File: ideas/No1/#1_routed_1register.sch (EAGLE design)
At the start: 20 parts, among them P1-O8RIGHT TD620831A, P1-P8LEFT TD620831A, U1 SN74HC595N, U2 SN74HC595N, U3 SN74HC595N

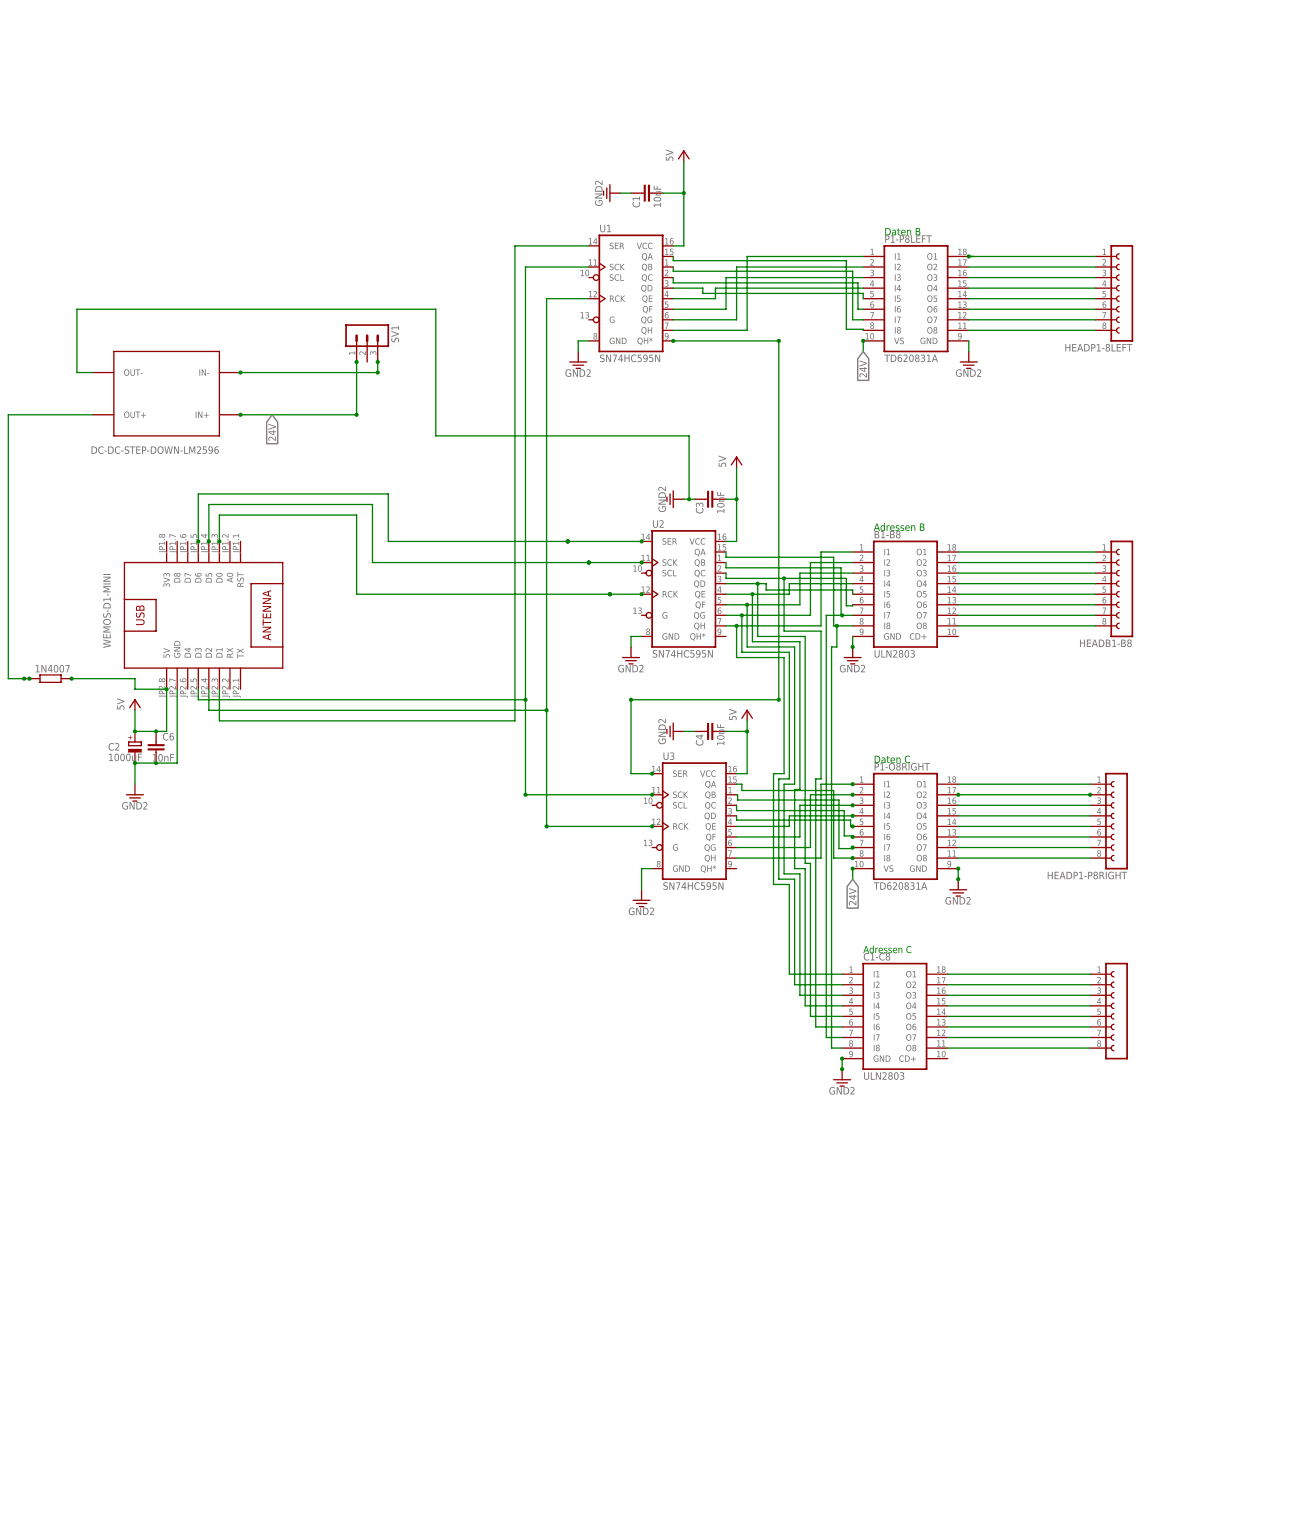
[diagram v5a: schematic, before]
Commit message: 1_route_1register.sch changed
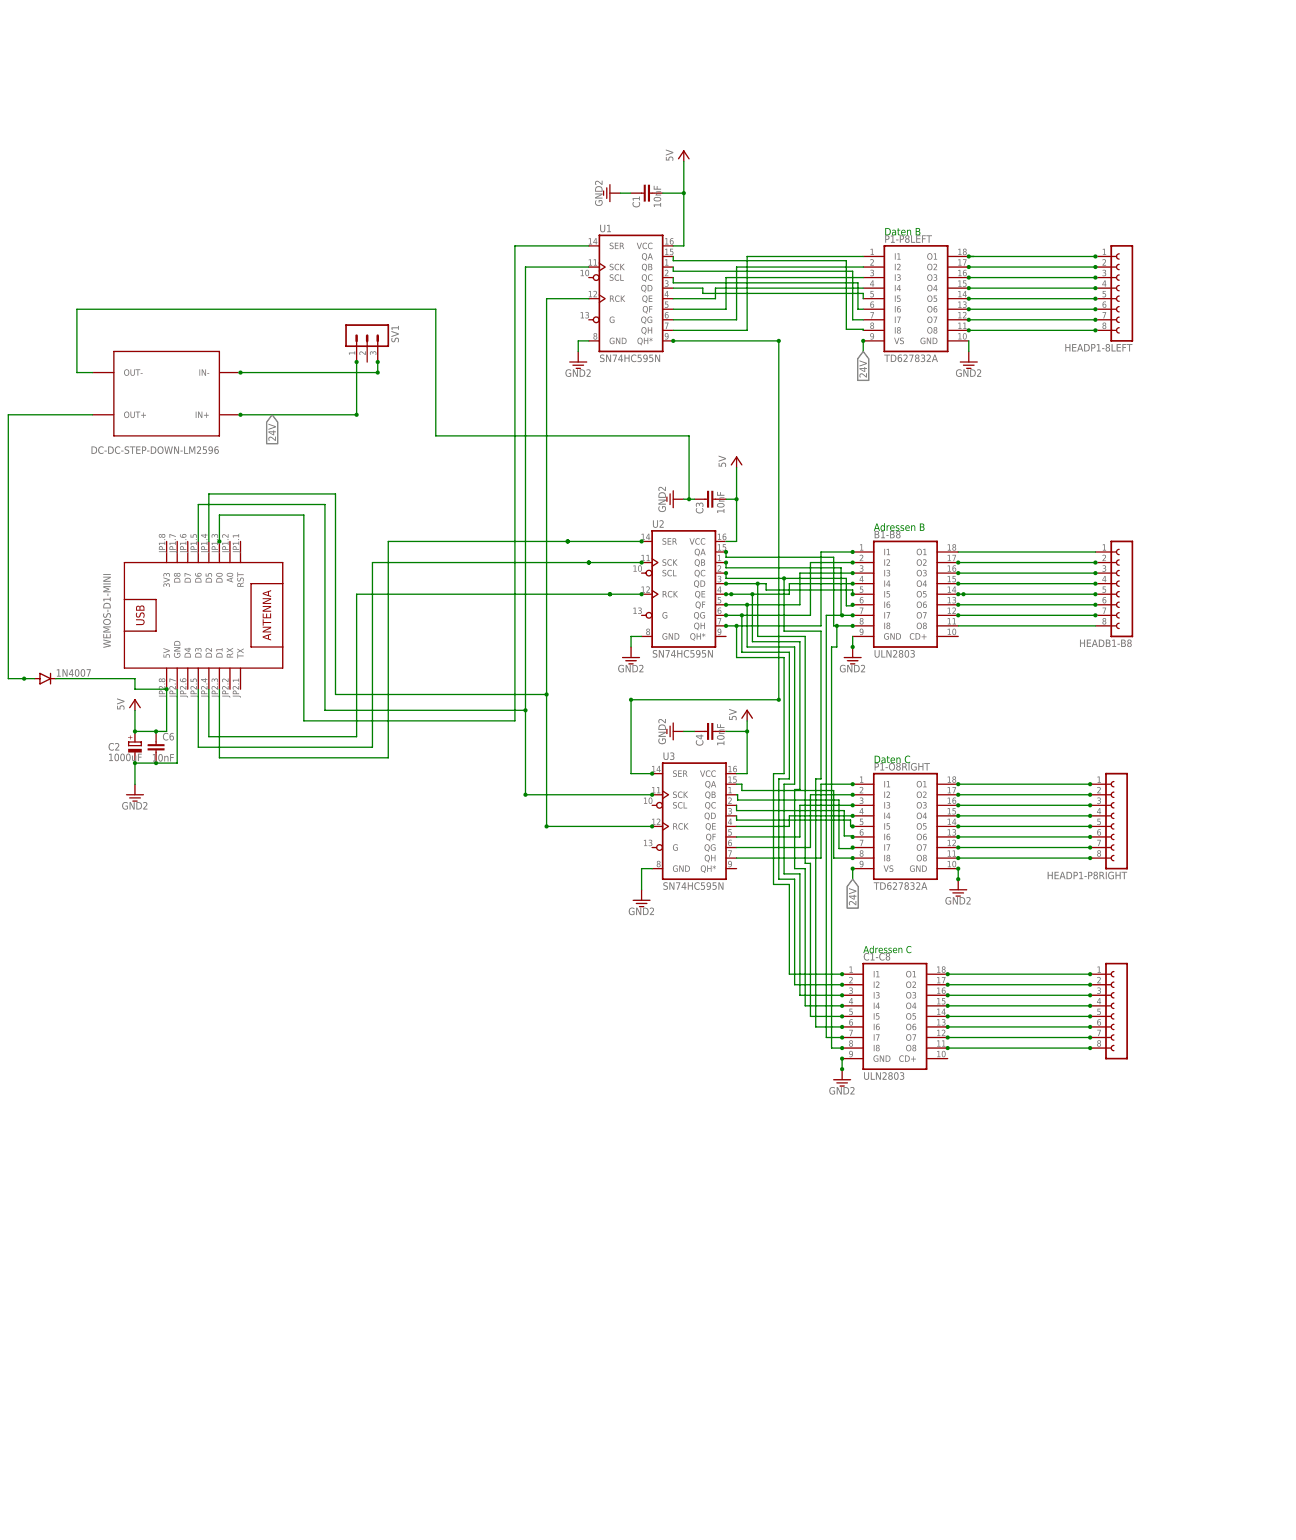
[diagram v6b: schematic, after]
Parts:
- 1N4007: device resistor:R-EU_0207/15 -> diode:DIODE-D-2.5
- P1-O8RIGHT, P1-P8LEFT: value TD620831A -> TD627832A; device td62083-dil:TD620831A -> td62083-dil:TD627832A
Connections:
- removed net N$36: U$1.D2, U1.RCK, U3.RCK
- removed net N$38: U$1.D0, U2.RCK
- new net N$74: U$1.D5, U1.RCK, U3.RCK
- new net N$76: U$1.D6, U1.SCK, U3.SCK
- net N$34: now also U$1.D0; no longer U$1.D1
- net N$37: now also U$1.D1; no longer U$1.D6
- net N$60: now also U$1.D2, U2.RCK; no longer U$1.D3, U1.SCK, U3.SCK
- net N$69: now also 1N4007.A; no longer 1N4007.1
- net N$80: now also U$1.D3; no longer U$1.D5
- net VCC: now also 1N4007.C; no longer 1N4007.2
